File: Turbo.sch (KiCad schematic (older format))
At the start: 16 parts, among them U12 74HCT27, U13 74HCT74, U14 74F86, U15 74F74, U16 74HCT04, U17 74HCT112, U18 74F157, U19 74F157

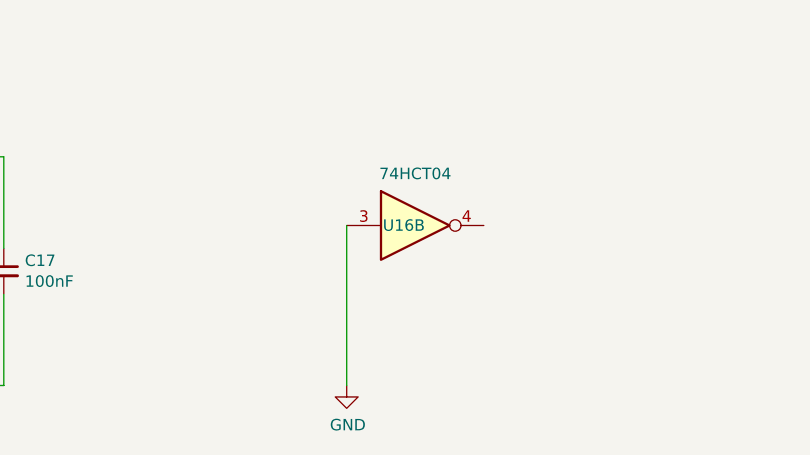
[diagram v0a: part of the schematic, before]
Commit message: fix bug with using second bank at C0
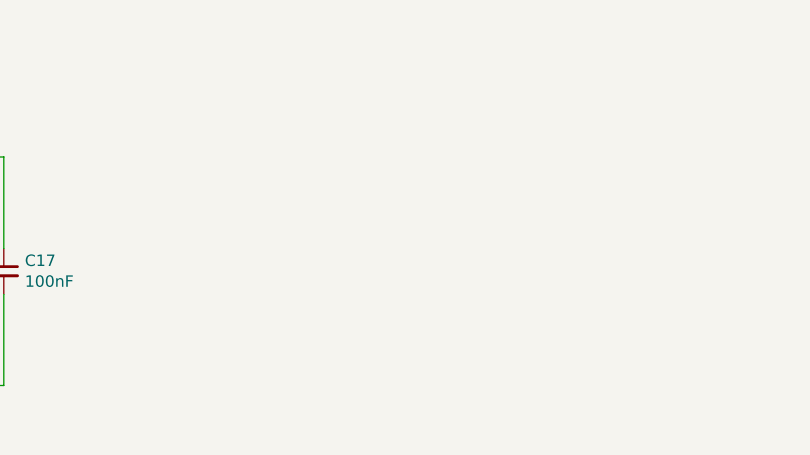
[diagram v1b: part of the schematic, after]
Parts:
- removed unit 2 of U16
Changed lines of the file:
@@
-$EndComp
-$Comp
-L 74:74HCT04 U16
-U 2 1 606DFD1C
-P 5550 6800
-F 0 "U16" H 5500 6800 50  0000 C CNN
-F 1 "74HCT04" H 5550 7026 50  0000 C CNN
-F 2 "Package_DIP:DIP-14_W7.62mm" H 5550 6800 50  0001 C CNN
-F 3 "https://assets.nexperia.com/documents/data-sheet/74HC_HCT04.pdf" H 5550 6800 50  0001 C CNN
-	2    5550 6800
-	1    0    0    -1
 $EndComp
 $Comp
@@
 Connection ~ 3450 6500
 $Comp
-L OpenAmiga2000CoproAdapter-rescue:GND-power #PWR?
-U 1 1 5FFA19F1
-P 5250 7500
-AR Path="/5FFA19F1" Ref="#PWR?"  Part="1"
-AR Path="/6068F728/5FFA19F1" Ref="#PWR?"  Part="1"
-AR Path="/606B7AE6/5FFA19F1" Ref="#PWR0141"  Part="1"
-F 0 "#PWR0141" H 5250 7250 50  0001 C CNN
-F 1 "GND" H 5255 7327 50  0000 C CNN
-F 2 "" H 5250 7500 50  0001 C CNN
-F 3 "" H 5250 7500 50  0001 C CNN
-	1    5250 7500
-	1    0    0    -1
-$EndComp
-$Comp
 L device:C_Small C18
 U 1 1 5FFA6B9B
@@
 	6700 1600 6800 1600
 Connection ~ 6700 1500
-Wire Wire Line
-	5250 6800 5250 7500
 $EndSCHEMATC

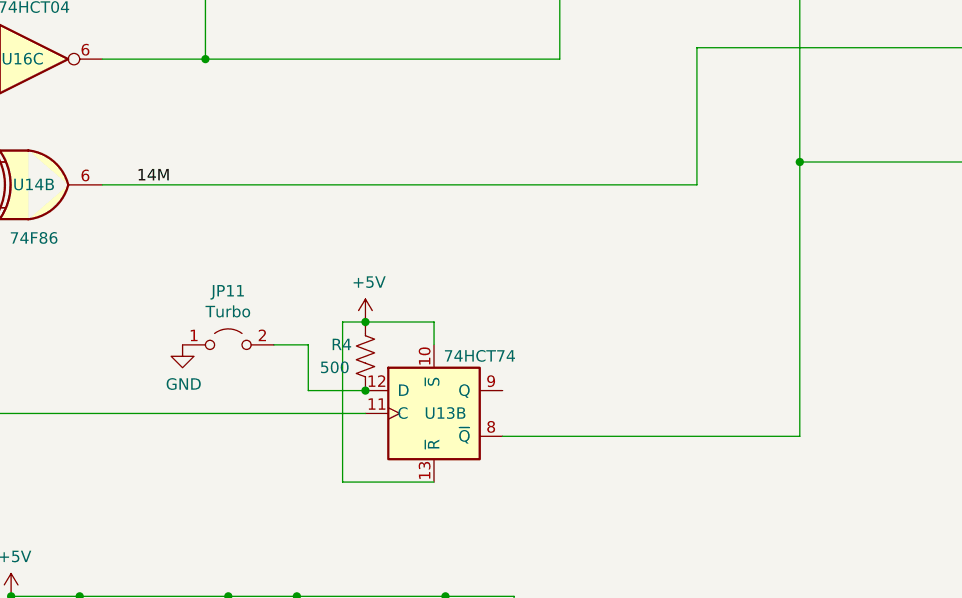
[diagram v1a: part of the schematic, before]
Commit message: reorganize turbo jumpers
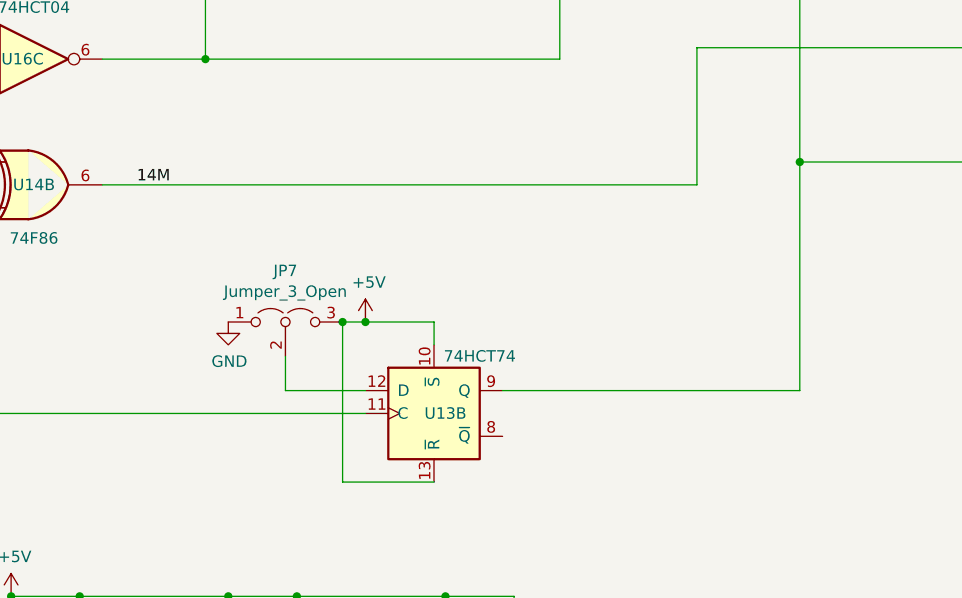
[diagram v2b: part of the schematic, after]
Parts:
- removed JP11: Turbo, Connector_PinHeader_2.54mm:PinHeader_1x02_P2.54mm_Vertical, symbol jumper:Jumper_2_Open
- removed R4: 500, Resistor_THT:R_Axial_DIN0411_L9.9mm_D3.6mm_P12.70mm_Horizontal, symbol device:R_US
- added JP7: Jumper_3_Open, Connector_PinHeader_2.54mm:PinHeader_1x03_P2.54mm_Vertical, symbol jumper:Jumper_3_Open
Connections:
- net +5V: now also JP7.3 (B)
- net GND: now also JP7.1 (A)
- net at U13.12 (D): now also JP7.2 (C)
- net at U18.1 (S), U19.1 (S): now also U13.9 (Q); no longer U13.8 (~Q)
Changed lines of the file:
@@
 	1250 4600 1250 5700
-$Comp
-L device:R_US R?
-U 1 1 60781007
-P 3100 5450
-AR Path="/6068F728/60781007" Ref="R?"  Part="1"
-AR Path="/606B7AE6/60781007" Ref="R4"  Part="1"
-F 0 "R4" H 2950 5500 50  0000 L CNN
-F 1 "500" H 2900 5400 50  0000 L CNN
-F 2 "Resistor_THT:R_Axial_DIN0411_L9.9mm_D3.6mm_P12.70mm_Horizontal" V 3140 5440 50  0001 C CNN
-F 3 "~" H 3100 5450 50  0001 C CNN
-	1    3100 5450
-	1    0    0    -1
-$EndComp
 $Comp
 L OpenAmiga2000CoproAdapter-rescue:+5V-power #PWR?
@@
 	3000 6000 3400 6000
 $Comp
-L jumper:Jumper_2_Open JP11
-U 1 1 60794674
-P 2500 5400
-F 0 "JP11" H 2500 5635 50  0000 C CNN
-F 1 "Turbo" H 2500 5544 50  0000 C CNN
-F 2 "Connector_PinHeader_2.54mm:PinHeader_1x02_P2.54mm_Vertical" H 2500 5400 50  0001 C CNN
-F 3 "~" H 2500 5400 50  0001 C CNN
-	1    2500 5400
-	1    0    0    -1
-$EndComp
-Wire Wire Line
-	2700 5400 2850 5400
-Wire Wire Line
-	2850 5400 2850 5600
-Wire Wire Line
-	2850 5600 3100 5600
-Connection ~ 3100 5600
-$Comp
 L OpenAmiga2000CoproAdapter-rescue:GND-power #PWR?
 U 1 1 6079922C
-P 2300 5400
+P 2500 5300
 AR Path="/6079922C" Ref="#PWR?"  Part="1"
 AR Path="/6068F728/6079922C" Ref="#PWR?"  Part="1"
 AR Path="/606B7AE6/6079922C" Ref="#PWR0129"  Part="1"
-F 0 "#PWR0129" H 2300 5150 50  0001 C CNN
-F 1 "GND" H 2305 5227 50  0000 C CNN
-F 2 "" H 2300 5400 50  0001 C CNN
-F 3 "" H 2300 5400 50  0001 C CNN
-	1    2300 5400
+F 0 "#PWR0129" H 2500 5050 50  0001 C CNN
+F 1 "GND" H 2505 5127 50  0000 C CNN
+F 2 "" H 2500 5300 50  0001 C CNN
+F 3 "" H 2500 5300 50  0001 C CNN
+	1    2500 5300
 	1    0    0    -1
 $EndComp
@@
 $EndComp
 Wire Wire Line
-	5000 5800 3700 5800
-Wire Wire Line
 	5000 2400 5000 4600
 Wire Wire Line
 	5000 4600 6800 4600
 Connection ~ 5000 4600
-Wire Wire Line
-	5000 4600 5000 5800
 Wire Wire Line
 	5000 2400 6800 2400
@@
 	6700 1600 6800 1600
 Connection ~ 6700 1500
+$Comp
+L jumper:Jumper_3_Open JP7
+U 1 1 64EEF7EF
+P 2750 5300
+F 0 "JP7" H 2750 5524 50  0000 C CNN
+F 1 "Jumper_3_Open" H 2750 5433 50  0000 C CNN
+F 2 "Connector_PinHeader_2.54mm:PinHeader_1x03_P2.54mm_Vertical" H 2750 5300 50  0001 C CNN
+F 3 "~" H 2750 5300 50  0001 C CNN
+	1    2750 5300
+	1    0    0    -1
+$EndComp
+Connection ~ 3000 5300
+Wire Wire Line
+	2750 5600 2750 5450
+Wire Wire Line
+	2750 5600 3100 5600
+Wire Wire Line
+	3700 5600 5000 5600
+Wire Wire Line
+	5000 4600 5000 5600
 $EndSCHEMATC

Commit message: more cleanup
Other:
- moved on the sheet: U12B, U15A
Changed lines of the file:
@@
 L 74:74HC74 U15
 U 1 1 606CEE81
-P 4250 3400
-F 0 "U15" H 4300 3400 50  0000 C CNN
-F 1 "74F74" H 4450 3650 50  0000 C CNN
-F 2 "Package_DIP:DIP-14_W7.62mm" H 4250 3400 50  0001 C CNN
-F 3 "74xx/74hc_hct74.pdf" H 4250 3400 50  0001 C CNN
-	1    4250 3400
+P 4250 3300
+F 0 "U15" H 4300 3300 50  0000 C CNN
+F 1 "74F74" H 4450 3550 50  0000 C CNN
+F 2 "Package_DIP:DIP-14_W7.62mm" H 4250 3300 50  0001 C CNN
+F 3 "74xx/74hc_hct74.pdf" H 4250 3300 50  0001 C CNN
+	1    4250 3300
 	1    0    0    -1
 $EndComp
@@
 U 4 1 606DE635
 P 1650 3100
-F 0 "U16" H 1650 3417 50  0000 C CNN
+F 0 "U16" H 1600 3100 50  0000 C CNN
 F 1 "74HCT04" H 1650 3326 50  0000 C CNN
 F 2 "Package_DIP:DIP-14_W7.62mm" H 1650 3100 50  0001 C CNN
@@
 L 74:74LS27 U12
 U 2 1 606EBC4F
-P 2500 1100
-F 0 "U12" H 2500 1100 50  0000 C CNN
-F 1 "74HCT27" H 2500 1334 50  0000 C CNN
-F 2 "Package_DIP:DIP-14_W7.62mm" H 2500 1100 50  0001 C CNN
-F 3 "http://www.ti.com/lit/gpn/sn74LS27" H 2500 1100 50  0001 C CNN
-	2    2500 1100
+P 2500 1300
+F 0 "U12" H 2500 1300 50  0000 C CNN
+F 1 "74HCT27" H 2500 1534 50  0000 C CNN
+F 2 "Package_DIP:DIP-14_W7.62mm" H 2500 1300 50  0001 C CNN
+F 3 "http://www.ti.com/lit/gpn/sn74LS27" H 2500 1300 50  0001 C CNN
+	2    2500 1300
 	1    0    0    -1
 $EndComp
 Wire Wire Line
 	3000 3300 3150 3300
-Wire Wire Line
-	3750 3200 3850 3200
-Wire Wire Line
-	3850 3200 3850 3300
-Wire Wire Line
-	3850 3300 3950 3300
 Wire Wire Line
 	3150 3200 3000 3200
@@
 	2200 3100 2700 3100
 Wire Wire Line
-	4250 3800 4250 3700
-Wire Wire Line
-	3950 4150 3950 3400
+	4250 3800 4250 3600
+Wire Wire Line
+	3950 4150 3950 3300
 Wire Wire Line
 	1950 4150 2400 4150
@@
 L OpenAmiga2000CoproAdapter-rescue:+5V-power #PWR?
 U 1 1 60718B8E
-P 4250 3100
+P 4250 3000
 AR Path="/60718B8E" Ref="#PWR?"  Part="1"
 AR Path="/6068F728/60718B8E" Ref="#PWR?"  Part="1"
 AR Path="/606B7AE6/60718B8E" Ref="#PWR0125"  Part="1"
-F 0 "#PWR0125" H 4250 2950 50  0001 C CNN
-F 1 "+5V" H 4265 3273 50  0000 C CNN
-F 2 "" H 4250 3100 50  0001 C CNN
-F 3 "" H 4250 3100 50  0001 C CNN
-	1    4250 3100
+F 0 "#PWR0125" H 4250 2850 50  0001 C CNN
+F 1 "+5V" H 4265 3173 50  0000 C CNN
+F 2 "" H 4250 3000 50  0001 C CNN
+F 3 "" H 4250 3000 50  0001 C CNN
+	1    4250 3000
 	1    0    0    -1
 $EndComp
@@
 	3100 1800 3100 2250
 Wire Wire Line
-	2200 1000 1000 1000
-Wire Wire Line
-	2100 2000 2100 1500
-Wire Wire Line
-	2100 1500 2800 1500
-Wire Wire Line
-	2800 1100 2800 1400
-Wire Wire Line
-	2200 1200 2200 1100
+	2500 1500 2800 1500
+Wire Wire Line
+	2800 1300 2800 1400
+Wire Wire Line
+	2200 1400 2200 1300
 Wire Wire Line
 	1700 1800 1350 1800
@@
 Wire Wire Line
 	2000 1400 2200 1400
-Wire Wire Line
-	2200 1400 2200 1200
-Connection ~ 2200 1200
+Connection ~ 2200 1400
 Wire Wire Line
 	2200 1400 2200 1900
-Connection ~ 2200 1400
 Text Notes 3150 2500 0    50   ~ 0
 Based on Amiga System Accelerator by\nLivio Plos and Jörg Richter
@@
 	2200 1900 6800 1900
 Wire Wire Line
-	4550 3500 5450 3500
+	4550 3400 5450 3400
 Wire Wire Line
 	6800 2100 6800 2200
@@
 	4550 4100 4550 4700
 Wire Wire Line
-	5450 3800 5450 3500
+	5450 3800 5450 3400
 Wire Wire Line
 	5450 3800 6800 3800
@@
 Wire Wire Line
 	5000 4600 5000 5600
+Wire Wire Line
+	3750 3200 3950 3200
+Wire Wire Line
+	2500 1500 2500 2000
+Wire Wire Line
+	2500 2000 2100 2000
+Wire Wire Line
+	1000 1000 2200 1000
+Wire Wire Line
+	2200 1000 2200 1200
 $EndSCHEMATC

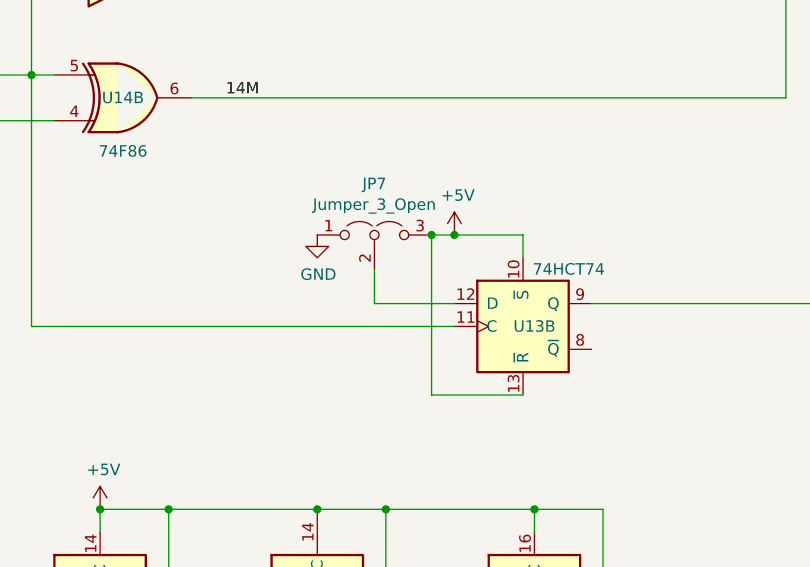
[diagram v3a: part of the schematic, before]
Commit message: add protection resistor
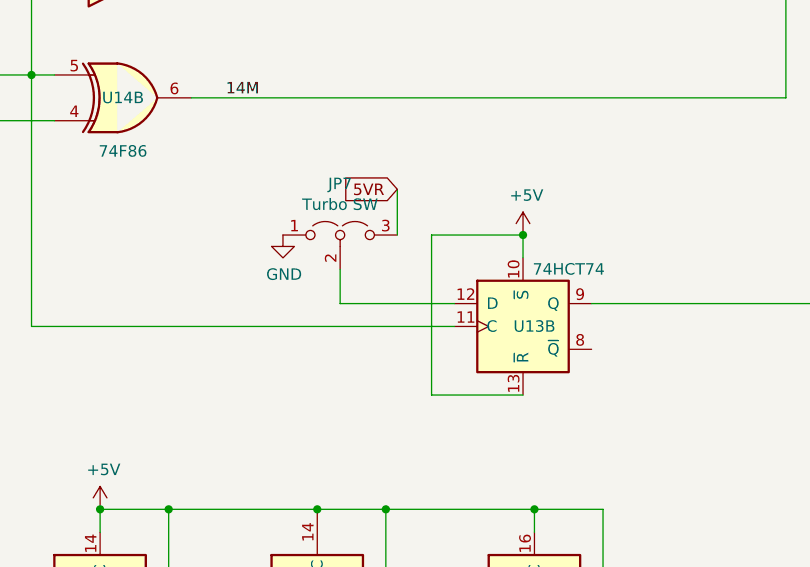
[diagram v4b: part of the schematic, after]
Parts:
- JP7: value Jumper_3_Open -> Turbo SW
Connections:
- net +5V: no longer JP7.3 (B)
- new net 5VR: JP7.3 (B)
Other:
- moved on the sheet: JP7
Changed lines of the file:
@@
 L OpenAmiga2000CoproAdapter-rescue:+5V-power #PWR?
 U 1 1 6078100D
-P 3100 5300
+P 3400 5300
 AR Path="/6078100D" Ref="#PWR?"  Part="1"
 AR Path="/6068F728/6078100D" Ref="#PWR?"  Part="1"
 AR Path="/606B7AE6/6078100D" Ref="#PWR0128"  Part="1"
-F 0 "#PWR0128" H 3100 5150 50  0001 C CNN
-F 1 "+5V" H 3115 5473 50  0000 C CNN
-F 2 "" H 3100 5300 50  0001 C CNN
-F 3 "" H 3100 5300 50  0001 C CNN
-	1    3100 5300
-	1    0    0    -1
-$EndComp
-Connection ~ 3100 5300
+F 0 "#PWR0128" H 3400 5150 50  0001 C CNN
+F 1 "+5V" H 3415 5473 50  0000 C CNN
+F 2 "" H 3400 5300 50  0001 C CNN
+F 3 "" H 3400 5300 50  0001 C CNN
+	1    3400 5300
+	1    0    0    -1
+$EndComp
 Wire Wire Line
 	1250 5700 3100 5700
-Wire Wire Line
-	3100 5300 3000 5300
-Wire Wire Line
-	3000 5300 3000 6000
 Wire Wire Line
 	3000 6000 3400 6000
@@
 L OpenAmiga2000CoproAdapter-rescue:GND-power #PWR?
 U 1 1 6079922C
-P 2500 5300
+P 2350 5300
 AR Path="/6079922C" Ref="#PWR?"  Part="1"
 AR Path="/6068F728/6079922C" Ref="#PWR?"  Part="1"
 AR Path="/606B7AE6/6079922C" Ref="#PWR0129"  Part="1"
-F 0 "#PWR0129" H 2500 5050 50  0001 C CNN
-F 1 "GND" H 2505 5127 50  0000 C CNN
-F 2 "" H 2500 5300 50  0001 C CNN
-F 3 "" H 2500 5300 50  0001 C CNN
-	1    2500 5300
+F 0 "#PWR0129" H 2350 5050 50  0001 C CNN
+F 1 "GND" H 2355 5127 50  0000 C CNN
+F 2 "" H 2350 5300 50  0001 C CNN
+F 3 "" H 2350 5300 50  0001 C CNN
+	1    2350 5300
 	1    0    0    -1
 $EndComp
@@
 Wire Wire Line
 	3400 5400 3400 5300
-Wire Wire Line
-	3100 5300 3400 5300
 $Comp
 L device:C_Small C17
@@
 L jumper:Jumper_3_Open JP7
 U 1 1 64EEF7EF
-P 2750 5300
-F 0 "JP7" H 2750 5524 50  0000 C CNN
-F 1 "Jumper_3_Open" H 2750 5433 50  0000 C CNN
-F 2 "Connector_PinHeader_2.54mm:PinHeader_1x03_P2.54mm_Vertical" H 2750 5300 50  0001 C CNN
-F 3 "~" H 2750 5300 50  0001 C CNN
-	1    2750 5300
-	1    0    0    -1
-$EndComp
-Connection ~ 3000 5300
-Wire Wire Line
-	2750 5600 2750 5450
-Wire Wire Line
-	2750 5600 3100 5600
+P 2600 5300
+F 0 "JP7" H 2600 5524 50  0000 C CNN
+F 1 "Turbo SW" H 2600 5433 50  0000 C CNN
+F 2 "Connector_PinHeader_2.54mm:PinHeader_1x03_P2.54mm_Vertical" H 2600 5300 50  0001 C CNN
+F 3 "~" H 2600 5300 50  0001 C CNN
+	1    2600 5300
+	1    0    0    -1
+$EndComp
+Wire Wire Line
+	2600 5600 2600 5450
+Wire Wire Line
+	2600 5600 3100 5600
 Wire Wire Line
 	3700 5600 5000 5600
@@
 Wire Wire Line
 	2200 1000 2200 1200
+Wire Wire Line
+	3000 6000 3000 5300
+Connection ~ 3400 5300
+Wire Wire Line
+	3000 5300 3400 5300
+Wire Wire Line
+	2850 5300 2850 5100
+Text GLabel 2850 5100 0    50   Input ~ 0
+5VR
 $EndSCHEMATC

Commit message: use digikey battery holder
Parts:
- U14: footprint Package_DIP:DIP-14_W7.62mm_Socket -> Package_DIP:DIP-14_W7.62mm
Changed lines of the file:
@@
 F 0 "U14" H 1650 4700 50  0000 C CNN
 F 1 "74F86" H 1650 4934 50  0000 C CNN
-F 2 "Package_DIP:DIP-14_W7.62mm_Socket" H 1650 4700 50  0001 C CNN
+F 2 "Package_DIP:DIP-14_W7.62mm" H 1650 4700 50  0001 C CNN
 F 3 "http://www.ti.com/lit/gpn/sn74HC86" H 1650 4700 50  0001 C CNN
 	2    1650 4700
